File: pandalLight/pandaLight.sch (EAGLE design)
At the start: 159 parts, among them J1 PJ-037A, U1 MIC23450AAAYML, U12 N25Q128AF8, U13 TPD12S016PWR, U14 AS4C128M16D3, U15 PMOD-2X6, U16 PMOD-2X6, U17 PLR135-T10, U18 PLT133-T10W, U19 PLR135-T10, U2 6SLX45CSG324, U20 TP10SQ, U21 TP10SQ, U22 PAN1322, U23 6SLX9TQG144, U3 TPD4S014SON, U4 FT2232HL, U5 93LC46BT-I/OT, U6 51, U7 51, U8 TPD12S016PWR, X1 USBUB-S, X2 HDMI_RECEPTICAL_A, X4 HDMI_RECEPTICAL_A, Y1 403, Y2 20Mhz

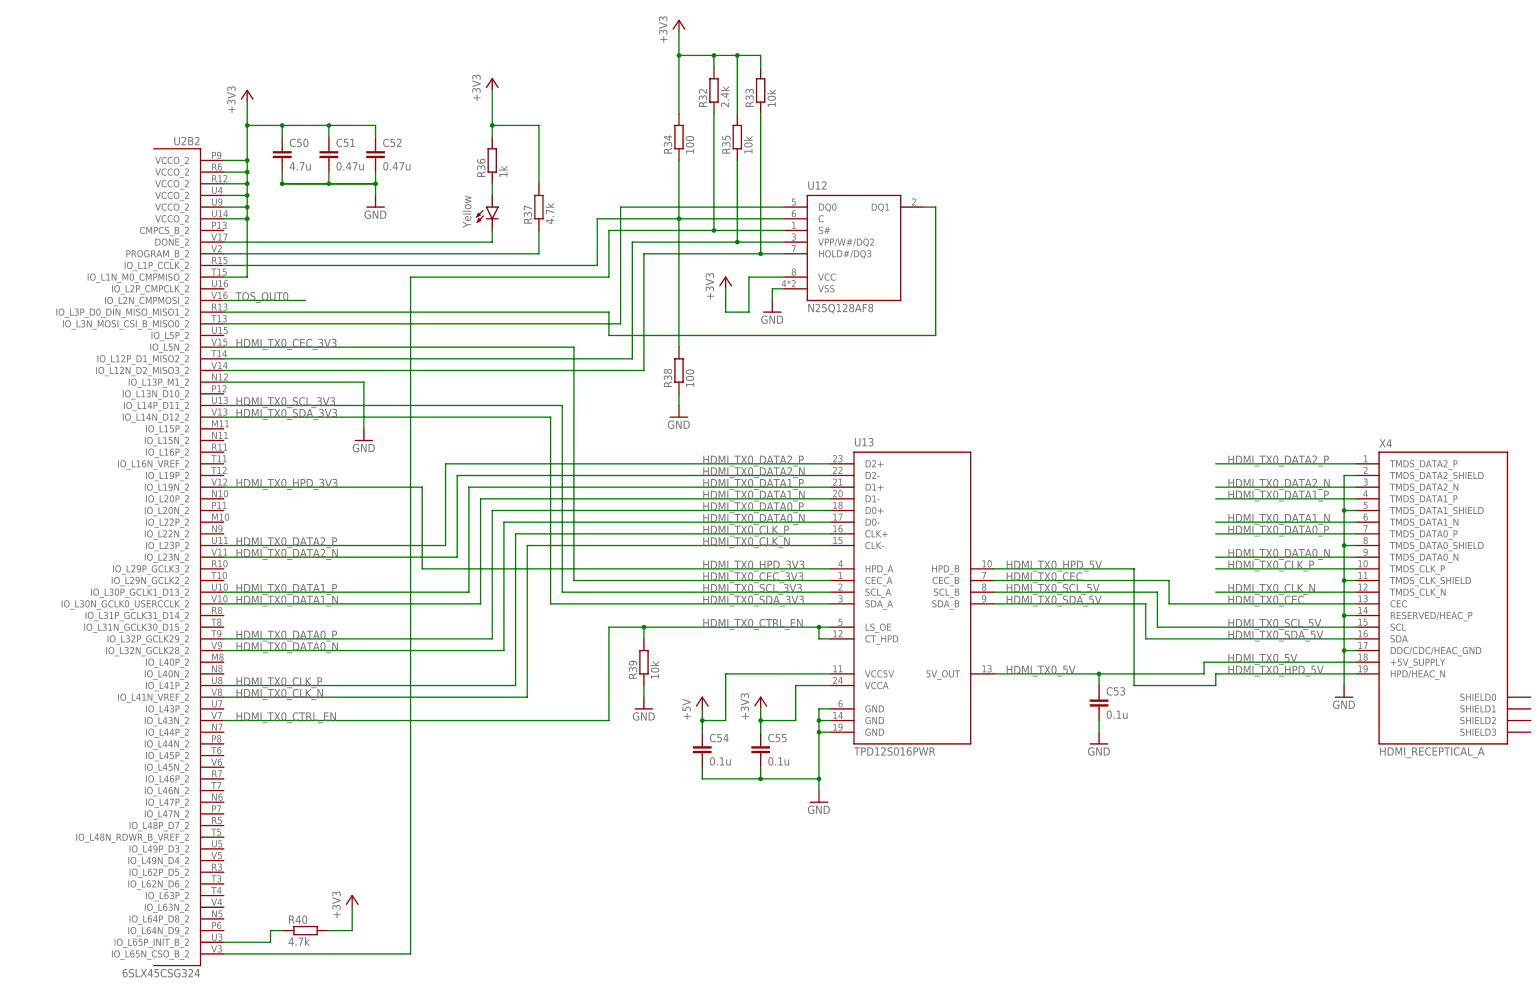
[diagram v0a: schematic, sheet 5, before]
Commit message: Continued switching to LX9
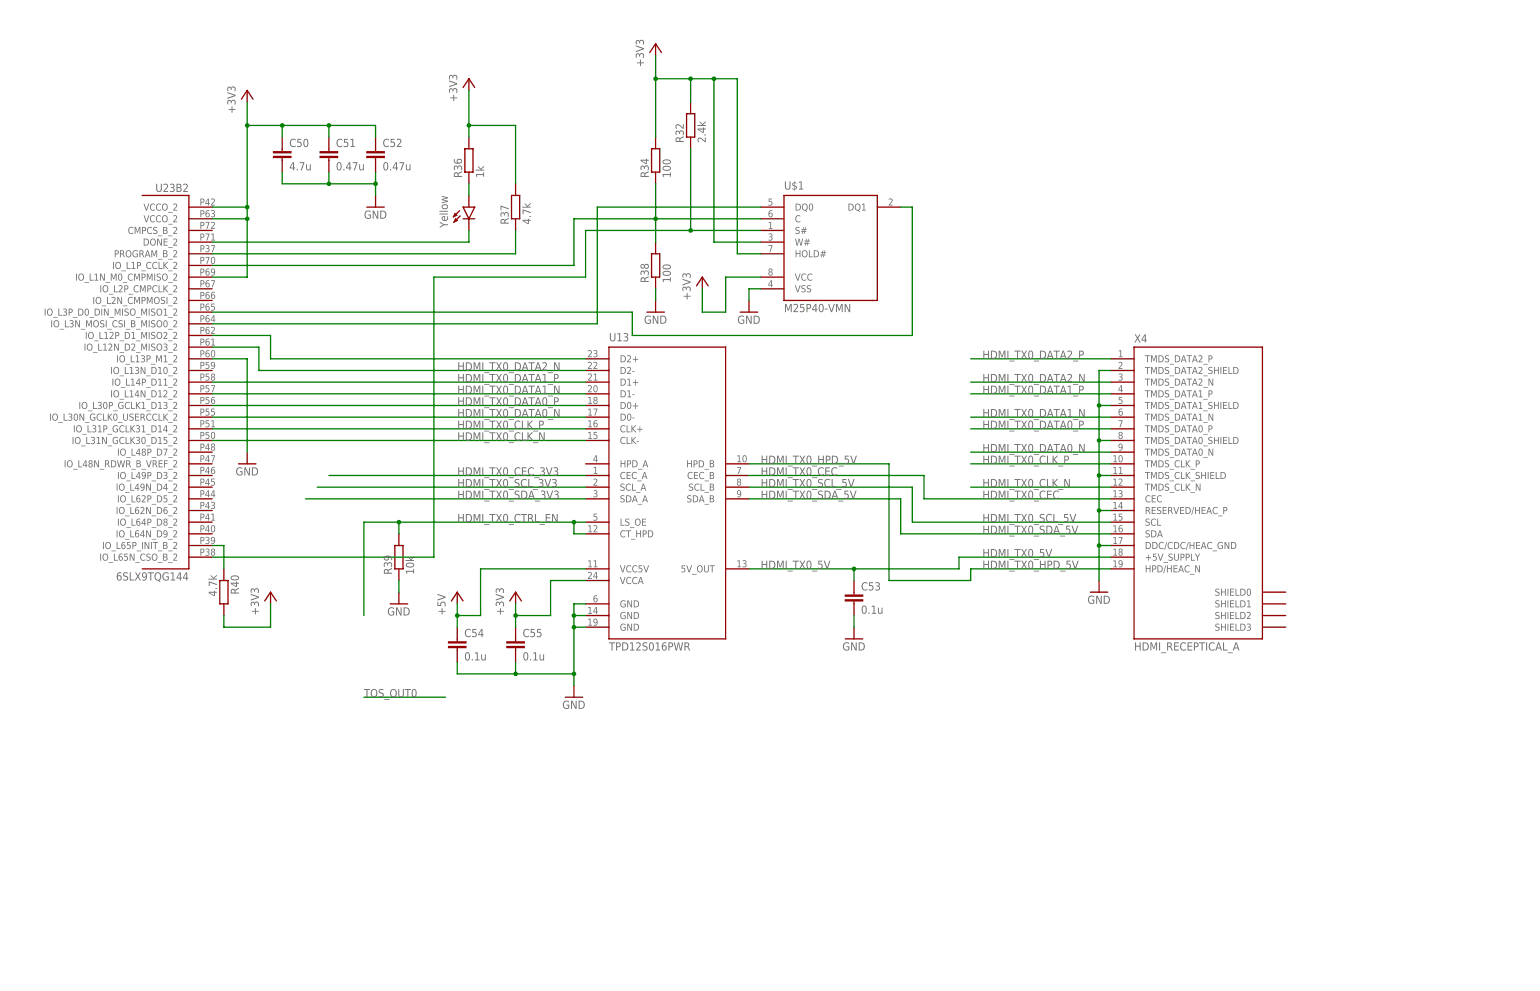
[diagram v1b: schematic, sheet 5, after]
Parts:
- removed C59, C60: 1u, pandaLight:CAPACITOR0402
- removed C61, C62, C63, C64, C65, C66, C72: 0.1u, pandaLight:CAPACITOR0402
- removed R33, R35: 10k, pandaLight:RESISTOR0402
- removed R41: 120, pandaLight:RESISTOR0402
- removed R42, R43: 4.7k, pandaLight:RESISTOR0402
- removed R44: 240, pandaLight:RESISTOR0402
- removed R45: 100, pandaLight:RESISTOR0402
- removed R46, R47: 1k, pandaLight:RESISTOR0402
- removed U12: N25Q128AF8, pandaLight:N25Q128AF8
- removed U14: AS4C128M16D3, pandaLight:AS4C128M16D3
- removed U2: 6SLX45CSG324, pandaLight:6SLX45CSG324
- added U$1: M25P40-VMN, pandaLight:M25P40-VMN
- R30, R31: value 220 -> 1k
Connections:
- removed net +1V5_VREF: C63.2, C64.1, C65.1, C66.1, C72.1, R46.1, R47.2, U14.VREFCA, U14.VREFDQ, U2B3.IO_L1N_VREF_3, U2B3.IO_L31N_VREF_3, U2B3.IO_L83N_VREF_3
- removed net DDR3_A0: U14.A0, U2B3.IO_L47P_M3A0_3
- removed net DDR3_A1: U14.A1, U2B3.IO_L47N_M3A1_3
- removed net DDR3_A10: U14.A10/AP, U2B3.IO_L51P_M3A10_3
- removed net DDR3_A11: U14.A11, U2B3.IO_L54N_M3A11_3
- removed net DDR3_A12: U14.A12/BC#, U2B3.IO_L53N_M3A12_3
- removed net DDR3_A2: U14.A2, U2B3.IO_L49N_M3A2_3
- removed net DDR3_A3: U14.A3, U2B3.IO_L45P_M3A3_3
- removed net DDR3_A4: U14.A4, U2B3.IO_L51N_M3A4_3
- removed net DDR3_A5: U14.A5, U2B3.IO_L44P_GCLK21_M3A5_3
- removed net DDR3_A6: U14.A6, U2B3.IO_L44N_GCLK20_M3A6_3
- removed net DDR3_A7: U14.A7, U2B3.IO_L49P_M3A7_3
- removed net DDR3_A8: U14.A8, U2B3.IO_L52P_M3A8_3
- removed net DDR3_A9: U14.A9, U2B3.IO_L52N_M3A9_3
- removed net DDR3_BA0: U14.BA0, U2B3.IO_L48P_M3BA0_3
- removed net DDR3_BA1: U14.BA1, U2B3.IO_L48N_M3BA1_3
- removed net DDR3_BA2: U14.BA2, U2B3.IO_L50N_M3BA2_3
- removed net DDR3_CAS#: U14.CAS#, U2B3.IO_L43N_GCLK22_IRDY2_M3CASN_3
- removed net DDR3_CK: R45.1, U14.CK, U2B3.IO_L46P_M3CLK_3
- removed net DDR3_CK#: R45.2, U14.CK#, U2B3.IO_L46N_M3CLKN_3
- removed net DDR3_CKE: R42.2, U14.CKE, U2B3.IO_L53P_M3CKE_3
- removed net DDR3_DQ0: U14.DQ0, U2B3.IO_L37P_M3DQ0_3
- removed net DDR3_DQ1: U14.DQ1, U2B3.IO_L37N_M3DQ1_3
- removed net DDR3_DQ10: U14.DQ10, U2B3.IO_L35P_M3DQ10_3
- removed net DDR3_DQ11: U14.DQ11, U2B3.IO_L35N_M3DQ11_3
- removed net DDR3_DQ12: U14.DQ12, U2B3.IO_L33P_M3DQ12_3
- removed net DDR3_DQ13: U14.DQ13, U2B3.IO_L33N_M3DQ13_3
- removed net DDR3_DQ14: U14.DQ14, U2B3.IO_L32P_M3DQ14_3
- removed net DDR3_DQ15: U14.DQ15, U2B3.IO_L32N_M3DQ15_3
- removed net DDR3_DQ2: U14.DQ2, U2B3.IO_L38P_M3DQ2_3
- removed net DDR3_DQ3: U14.DQ3, U2B3.IO_L38N_M3DQ3_3
- removed net DDR3_DQ4: U14.DQ4, U2B3.IO_L41P_GCLK27_M3DQ4_3
- removed net DDR3_DQ5: U14.DQ5, U2B3.IO_L41N_GCLK26_M3DQ5_3
- removed net DDR3_DQ6: U14.DQ6, U2B3.IO_L40P_M3DQ6_3
- removed net DDR3_DQ7: U14.DQ7, U2B3.IO_L40N_M3DQ7_3
- removed net DDR3_DQ8: U14.DQ8, U2B3.IO_L36P_M3DQ8_3
- removed net DDR3_DQ9: U14.DQ9, U2B3.IO_L36N_M3DQ9_3
- removed net DDR3_LDM: U14.LDM, U2B3.IO_L42N_GCLK24_M3LDM_3
- removed net DDR3_LDQS: U14.LDQS, U2B3.IO_L39P_M3LDQS_3
- removed net DDR3_LDQS#: U14.LDQS#, U2B3.IO_L39N_M3LDQSN_3
- removed net DDR3_ODT: U14.ODT, U2B3.IO_L45N_M3ODT_3
- removed net DDR3_RAS#: U14.RAS#, U2B3.IO_L43P_GCLK23_M3RASN_3
- removed net DDR3_RESET#: R43.2, U14.RESET#, U2B3.IO_L54P_M3RESET_3
- removed net DDR3_UDM: U14.UDM, U2B3.IO_L42P_GCLK25_TRDY2_M3UDM_3
- removed net DDR3_UDQS: U14.UDQS, U2B3.IO_L34P_M3UDQS_3
- removed net DDR3_UDQS#: U14.UDQS#, U2B3.IO_L34N_M3UDQSN_3
- removed net DDR3_WE#: U14.WE#, U2B3.IO_L50P_M3WE_3
- removed net HDMI_TX0_HPD_3V3: U13.HPD_A, U2B2.IO_L19N_2
- removed net M3_RZQ: R41.1, U2B3.IO_L31P_3
- removed net N$46: R33.1, U12.HOLD#/DQ3, U2B2.IO_L12N_D2_MISO3_2
- removed net N$53: LED4.C, R31.2
- net +1V5: no longer C59.1, C60.1, C61.1, C62.1, C63.1, R46.2, U14.VDD@B2, U14.VDD@D9, U14.VDD@G7, U14.VDD@K2, U14.VDD@K8, U14.VDD@N1, U14.VDD@N9, U14.VDD@R1, U14.VDD@R9, U14.VDDQ@A1, U14.VDDQ@A8, U14.VDDQ@C1, U14.VDDQ@C9, U14.VDDQ@D2, U14.VDDQ@E9, U14.VDDQ@F1, U14.VDDQ@H2, U14.VDDQ@H9, U2B3.VCCO_3@0, U2B3.VCCO_3@1, U2B3.VCCO_3@2, U2B3.VCCO_3@3, U2B3.VCCO_3@4, U2B3.VCCO_3@5
- net +3V3: now also R30.2, R31.2, U$1.HOLD#, U$1.VCC, U$1.W#, U23B0.VCCO_0@0, U23B0.VCCO_0@1, U23B0.VCCO_0@2, U23B1.VCCO_1@0, U23B1.VCCO_1@1, U23B1.VCCO_1@2, U23B2.IO_L1N_M0_CMPMISO_2, U23B2.VCCO_2@0, U23B2.VCCO_2@1; no longer LED3.A, LED4.A, R33.2, R35.2, U12.VCC, U2B2.IO_L1N_M0_CMPMISO_2, U2B2.VCCO_2@0, U2B2.VCCO_2@1, U2B2.VCCO_2@2, U2B2.VCCO_2@3, U2B2.VCCO_2@4, U2B2.VCCO_2@5
- net GND: now also U$1.VSS, U23B2.IO_L13P_M1_2; no longer C59.2, C60.2, C61.2, C62.2, C64.2, C65.2, C66.2, C72.2, R41.2, R42.1, R43.1, R44.1, R47.1, U12.VSS, U14.CS#, U14.VSS@A9, U14.VSS@B3, U14.VSS@E1, U14.VSS@G8, U14.VSS@J2, U14.VSS@J8, U14.VSS@M1, U14.VSS@M9, U14.VSS@P1, U14.VSS@P9, U14.VSS@T1, U14.VSS@T9, U14.VSSQ@B1, U14.VSSQ@B9, U14.VSSQ@D1, U14.VSSQ@D8, U14.VSSQ@E2, U14.VSSQ@E8, U14.VSSQ@F9, U14.VSSQ@G1, U14.VSSQ@G9, U2B2.IO_L13P_M1_2
- net HDMI_TX0_CEC_3V3: no longer U2B2.IO_L5N_2
- net HDMI_TX0_CLK_N: now also U23B2.IO_L31N_GCLK30_D15_2; no longer U2B2.IO_L41N_VREF_2
- net HDMI_TX0_CLK_P: now also U23B2.IO_L31P_GCLK31_D14_2; no longer U2B2.IO_L41P_2
- net HDMI_TX0_CTRL_EN: no longer U2B2.IO_L43N_2
- net HDMI_TX0_DATA0_N: now also U23B2.IO_L30N_GCLK0_USERCCLK_2; no longer U2B2.IO_L32N_GCLK28_2
- net HDMI_TX0_DATA0_P: now also U23B2.IO_L30P_GCLK1_D13_2; no longer U2B2.IO_L32P_GCLK29_2
- net HDMI_TX0_DATA1_N: now also U23B2.IO_L14N_D12_2; no longer U2B2.IO_L30N_GCLK0_USERCCLK_2
- net HDMI_TX0_DATA1_P: now also U23B2.IO_L14P_D11_2; no longer U2B2.IO_L30P_GCLK1_D13_2
- net HDMI_TX0_DATA2_N: now also U23B2.IO_L12N_D2_MISO3_2; no longer U2B2.IO_L23N_2
- net HDMI_TX0_DATA2_P: no longer U13.D2+, U2B2.IO_L23P_2
- net HDMI_TX0_SCL_3V3: no longer U2B2.IO_L14P_D11_2
- net HDMI_TX0_SDA_3V3: no longer U2B2.IO_L14N_D12_2
- net N$3: now also LED4.A, R31.1; no longer R44.2, U14.ZQ
- net N$33: now also U23B2.DONE_2; no longer U2B2.DONE_2
- net N$34: now also U23B2.PROGRAM_B_2; no longer U2B2.PROGRAM_B_2
- net N$35: now also U23B0.IO_L1P_HSWAPEN_0
- net N$37: now also LED3.A, R30.1; no longer LED3.C, R30.2
- net N$39: now also U23B2.IO_L65P_INIT_B_2; no longer U2B2.IO_L65P_INIT_B_2
- net N$40: now also U$1.DQ0, U23B2.IO_L3N_MOSI_CSI_B_MISO0_2; no longer U12.DQ0, U2B2.IO_L3N_MOSI_CSI_B_MISO0_2
- net N$41: now also U$1.S#, U23B2.IO_L65N_CSO_B_2; no longer U12.S#, U2B2.IO_L65N_CSO_B_2
- net N$42: now also U$1.C, U23B2.IO_L1P_CCLK_2; no longer U12.C, U2B2.IO_L1P_CCLK_2
- net N$43: now also U$1.DQ1, U23B2.IO_L3P_D0_DIN_MISO_MISO1_2; no longer U12.DQ1, U2B2.IO_L3P_D0_DIN_MISO_MISO1_2
- net N$44: now also U13.D2+, U23B2.IO_L12P_D1_MISO2_2; no longer R35.1, U12.VPP/W#/DQ2, U2B2.IO_L12P_D1_MISO2_2
- net TOS_OUT0: no longer U2B2.IO_L2N_CMPMOSI_2
- net USB_CTS#: now also U23B0.IO_L66N_SCP0_0
- net USB_DCD#: now also U23B0.IO_L63N_SCP6_0
- net USB_DSR#: now also U23B0.IO_L64P_SCP5_0
- net USB_DTR#: now also U23B0.IO_L64N_SCP4_0
- net USB_RI#: now also U23B0.IO_L63P_SCP7_0
- net USB_RTS#: now also U23B0.IO_L66P_SCP1_0
- net USB_RXD: now also U23B0.IO_L65N_SCP2_0
- net USB_RXLED#: now also LED3.C; no longer R30.1
- net USB_TXD: now also U23B0.IO_L65P_SCP3_0
- net USB_TXLED#: now also LED4.C; no longer R31.1
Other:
- note removed: "NEEDS A DIFFERENTIAL CLOCK INPUT!"
- moved on the sheet: C37, C38, C39, C53, C54, C55, C56, C57, C58, R27, R30, R31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

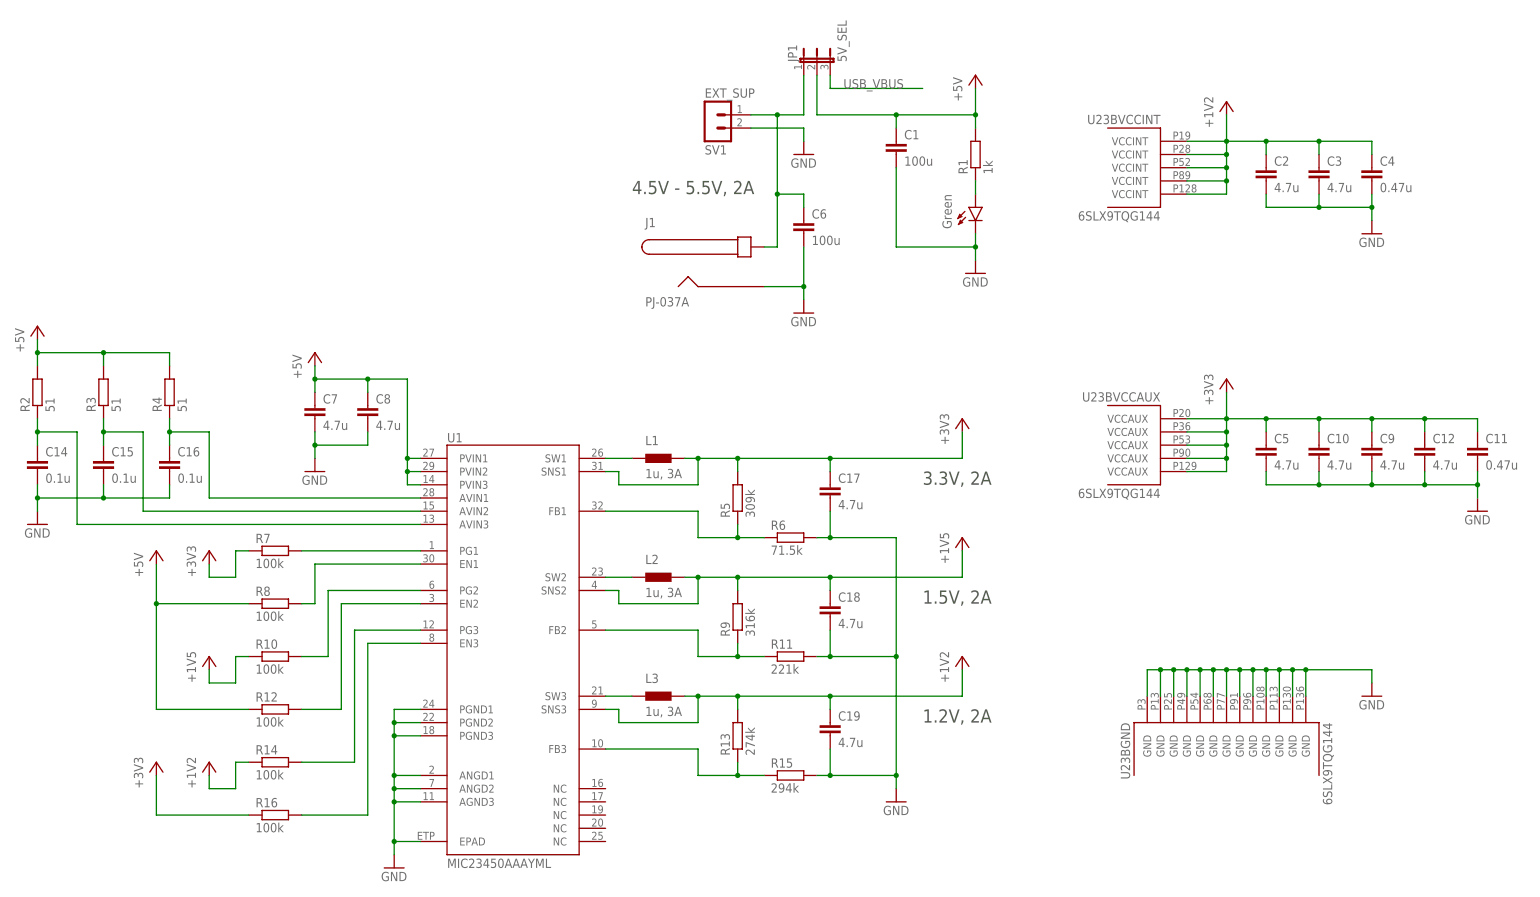
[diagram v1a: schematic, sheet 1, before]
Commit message: Made new signal connections; Removed old signals; New buck regulator; Reset the board layout
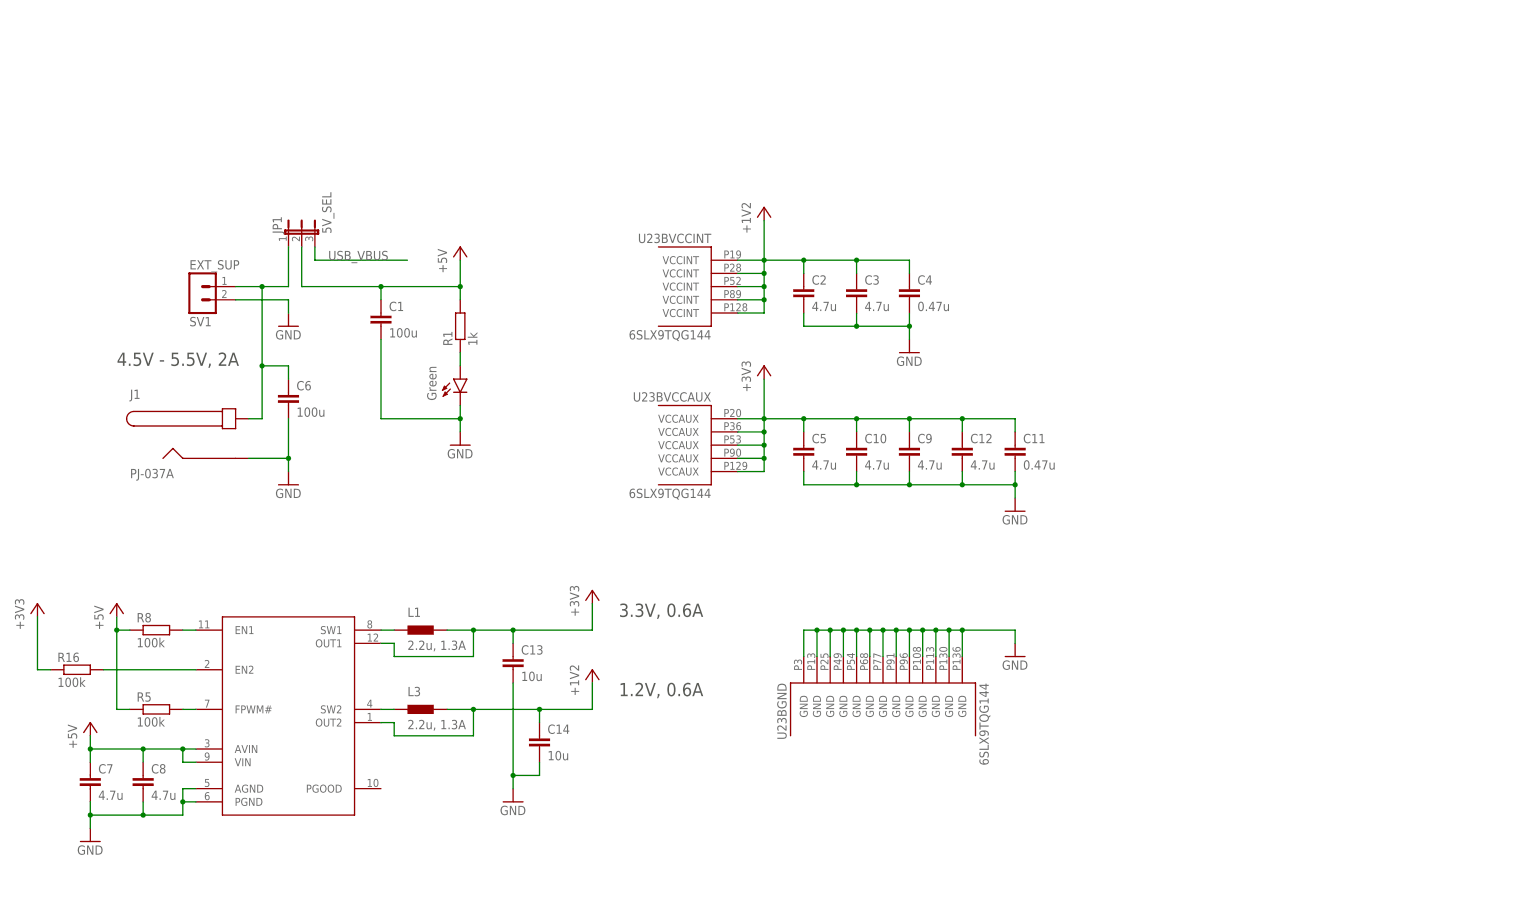
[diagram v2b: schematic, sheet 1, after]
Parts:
- removed C15, C16, C69: 0.1u, pandaLight:CAPACITOR0402
- removed C17, C18, C19: 4.7u, pandaLight:CAPACITOR0603
- removed L2: 1u, 3A, pandaLight:INDUCTOR1008
- removed L5: 47u, pandaLight:INDUCTOR0603
- removed R10, R12, R14, R7: 100k, pandaLight:RESISTOR0402
- removed R11: 221k, pandaLight:RESISTOR0402
- removed R13: 274k, pandaLight:RESISTOR0402
- removed R15: 294k, pandaLight:RESISTOR0402
- removed R2, R3, R4: 51, pandaLight:RESISTOR0402
- removed R6: 71.5k, pandaLight:RESISTOR0402
- removed R9: 316k, pandaLight:RESISTOR0402
- removed U1: MIC23450AAAYML, pandaLight:MIC23450AAAYML
- removed U19: PLR135-T10, pandaLight:PLR135-T10
- added C13: 10u, pandaLight:CAPACITOR0603
- added SV3: (no value), pandaLight:MA02-1
- added U$2: MIC2230-XXYML, pandaLight:MIC2230-XXYML
- C14: value 0.1u -> 10u; device pandaLight:CAPACITOR0402 -> pandaLight:CAPACITOR0603; PARTNO CL05B104KP5NNNC -> (none)
- L1, L3: value 1u, 3A -> 2.2u, 1.3A
- R5: value 309k -> 100k; PARTNO ERJ-2RKF3093X -> ERJ-2RKF1003X
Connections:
- removed net FPGA_OSC1: Y2.OUT
- removed net N$14: L1.1, U1.SW1
- removed net N$15: C16.1, R4.1, U1.AVIN1
- removed net N$16: L2.1, U1.SW2
- removed net N$17: L3.1, U1.SW3
- removed net N$18: R13.1, R15.1, U1.FB3
- removed net N$20: R10.2, U1.PG2
- removed net N$21: R5.1, R6.1, U1.FB1
- removed net N$22: R7.2, U1.PG1
- removed net N$23: R11.1, R9.1, U1.FB2
- removed net N$24: R12.2, U1.EN2
- removed net N$26: R14.2, U1.PG3
- removed net N$30: C15.1, R3.1, U1.AVIN2
- removed net N$48: C14.1, R2.1, U1.AVIN3
- removed net TOS_IN1: U19.VOUT
- new net FPGA_CLK20: U23B3.IO_L42N_GCLK24_3, Y2.OUT
- new net LEDS_CLK: SV3.2, U23B3.IO_L52N_3
- new net LEDS_DATA: SV3.1, U23B3.IO_L52P_3
- new net SW1: L1.1, U$2.SW1
- new net SW2: L3.1, U$2.SW2
- net +1V2: now also C14.1, U$2.OUT2; no longer C19.1, R13.2, R14.1, U1.SNS3
- net +1V5: now also U23B3.VCCO_3@0, U23B3.VCCO_3@1, U23B3.VCCO_3@2; no longer C18.1, L2.2, R10.1, R9.2, U1.SNS2
- net +3V3: now also C13.1, U$2.OUT1; no longer C17.1, L5.1, R5.2, R7.1, U1.SNS1
- net +5V: now also R5.1, U$2.AVIN, U$2.VIN; no longer R12.1, R2.2, R3.2, R4.2, U1.PVIN1, U1.PVIN2, U1.PVIN3
- net GND: now also C13.2, U$2.AGND, U$2.PGND; no longer C15.2, C16.2, C17.2, C18.2, C19.2, C69.2, R11.2, R15.2, R6.2, U1.AGND3, U1.ANGD1, U1.ANGD2, U1.EPAD, U1.PGND1, U1.PGND2, U1.PGND3, U19.GND
- net HDMI_TX0_CEC_3V3: now also U23B2.IO_L48P_D7_2
- net HDMI_TX0_CTRL_EN: now also U23B2.IO_L49N_D4_2
- net HDMI_TX0_SCL_3V3: now also U23B2.IO_L48N_RDWR_B_VREF_2
- net HDMI_TX0_SDA_3V3: now also U23B2.IO_L49P_D3_2
- net N$25: now also U$2.EN1; no longer U1.EN1
- net N$27: now also U$2.EN2; no longer U1.EN3
- net N$4: now also R5.2, U$2.FPWM#; no longer C69.1, L5.2, U19.VCC
- net TOS_IN0: now also U23B0.IO_L37P_GCLK13_0
- net TOS_OUT0: now also U23B2.IO_L62P_D5_2
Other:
- note added: "1.2V, 0.6A"
- note added: "3.3V, 0.6A"
- note removed: "1.2V, 2A"
- note removed: "1.5V, 2A"
- note removed: "3.3V, 2A"
- moved on the sheet: C1, C10, C11, C12, C14, C2, C3, C37, C38, C39, C4, C40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
